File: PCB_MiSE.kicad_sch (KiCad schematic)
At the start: 40 parts, among them IC1 MSP430FR2355TPT, J1 WIFI, J10 Conn_01x01, J11 Conn_01x01, J2 Conn_01x03, J3 Conn_01x01, J4 Clk read conn, J5 Conn_01x01, J6 Display, J7 Conn_01x01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

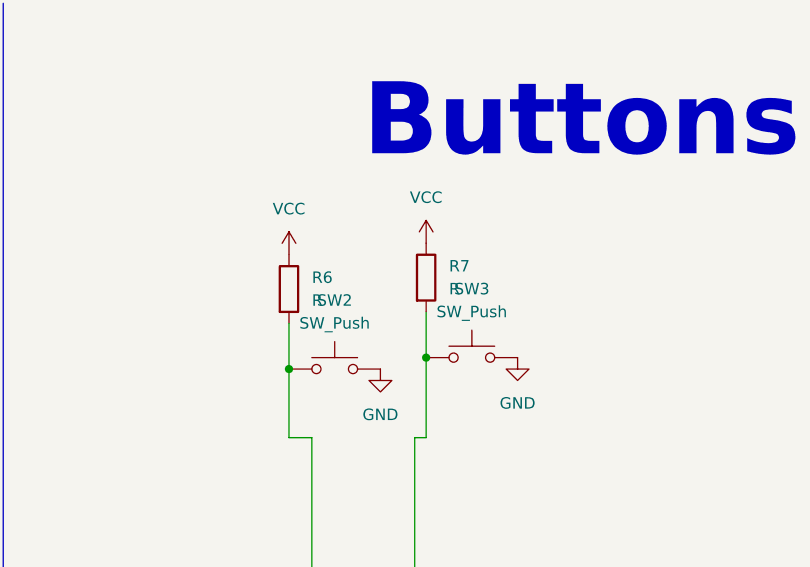
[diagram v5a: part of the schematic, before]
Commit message: falta cambiar pulsadores
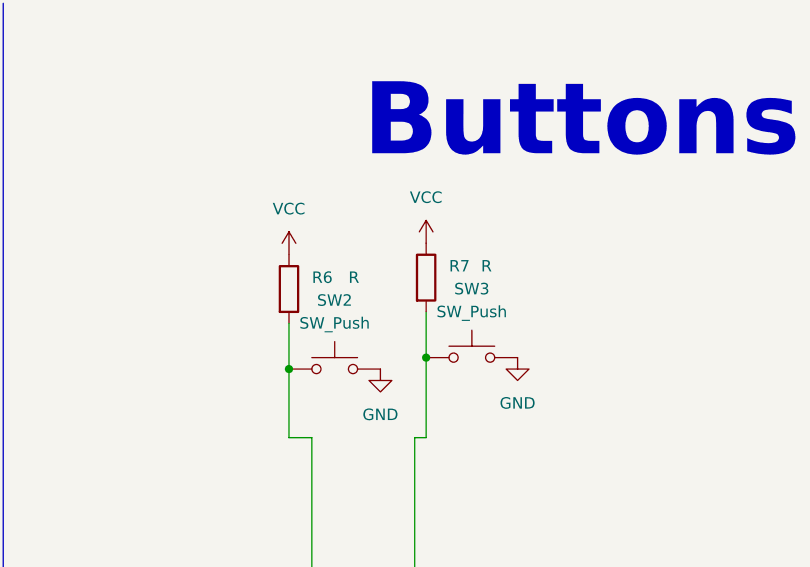
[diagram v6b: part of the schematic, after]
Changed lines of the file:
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@@
 		)
 		(instances
-			(project ""
+			(project "PCB_MiSE"
 				(path "/d767662d-a2fb-4431-89c7-c67b7c23601b"
 					(reference "SW1")
@@
 		(on_board yes)
 		(dnp no)
-		(fields_autoplaced yes)
 		(property "Reference" "R6"
 			(at 323.85 43.1799 0)
@@
 		)
 		(property "Value" "R"
-			(at 323.85 45.7199 0)
+			(at 327.914 43.18 0)
 			(effects
 				(font
@@
 		(on_board yes)
 		(dnp no)
-		(fields_autoplaced yes)
 		(property "Reference" "R7"
 			(at 339.09 41.9099 0)
@@
 		)
 		(property "Value" "R"
-			(at 339.09 44.4499 0)
-			(effects
-				(font
+			(at 342.646 41.91 0)
+			(effects
+				(font

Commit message: MiSE 13/3
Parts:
- R1, R10, R5, R9: value R -> 10k
- R12, R13: value R -> 2k2
- R14, R6, R7: value R -> 1k
- R2: value R -> 31k
- R3: value R -> 20k
- R4: value R -> 47k
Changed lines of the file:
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@@
 			(width 0)
 			(type default)
+			(color 255 0 0 1)
 		)
 	)
@@
 			(width 0)
 			(type default)
+			(color 255 0 0 1)
 		)
 	)
@@
 			(width 0)
 			(type default)
+			(color 255 0 0 1)
 		)
 	)
@@
 			(width 0)
 			(type default)
+			(color 255 0 0 1)
 		)
 	)
@@
 			(width 0)
 			(type default)
+			(color 255 0 0 1)
 		)
 	)
@@
 			(width 0)
 			(type default)
+			(color 255 0 0 1)
 		)
 	)
@@
 			(width 0)
 			(type default)
+			(color 255 0 0 1)
 		)
 	)
@@
 			(width 0)
 			(type default)
+			(color 255 0 0 1)
 		)
 	)
@@
 			(width 0)
 			(type default)
+			(color 255 0 0 1)
 		)
 	)
@@
 			(width 0)
 			(type default)
+			(color 255 0 0 1)
 		)
 	)
@@
 			(width 0)
 			(type default)
+			(color 255 0 0 1)
 		)
 	)
@@
 			(width 0)
 			(type default)
+			(color 255 0 0 1)
 		)
 	)
@@
 			(width 0)
 			(type default)
+			(color 255 0 0 1)
 		)
 	)
@@
 			(width 0)
 			(type default)
+			(color 255 0 0 1)
 		)
 	)
@@
 			(width 0)
 			(type default)
+			(color 255 0 0 1)
 		)
 	)
@@
 			(width 0)
 			(type default)
+			(color 255 0 0 1)
 		)
 	)
@@
 			(width 0)
 			(type default)
+			(color 255 0 0 1)
 		)
 	)
@@
 			(width 0)
 			(type default)
+			(color 255 0 0 1)
 		)
 	)
@@
 			(width 0)
 			(type default)
+			(color 255 0 0 1)
 		)
 	)
@@
 			(width 0)
 			(type default)
+			(color 255 0 0 1)
 		)
 	)
@@
 			(width 0)
 			(type default)
+			(color 255 0 0 1)
 		)
 	)
@@
 			)
 		)
-		(property "Value" "R"
+		(property "Value" "2k2"
 			(at 241.3 186.6899 0)
 			(effects
@@
 			)
 		)
-		(property "Value" "R"
+		(property "Value" "1k"
 			(at 327.914 43.18 0)
 			(effects
@@
 			)
 		)
-		(property "Value" "R"
+		(property "Value" "10k"
 			(at 214.63 87.6299 0)
 			(effects
@@
 		(lib_id "Device:R")
 		(at 29.21 344.17 0)
+		(mirror y)
 		(unit 1)
 		(exclude_from_sim no)
@@
 		(on_board yes)
 		(dnp no)
-		(fields_autoplaced yes)
 		(property "Reference" "R3"
-			(at 31.75 342.8999 0)
+			(at 26.67 342.8999 0)
 			(effects
 				(font
@@
 			)
 		)
-		(property "Value" "R"
-			(at 31.75 345.4399 0)
+		(property "Value" "20k"
+			(at 26.67 345.4399 0)
 			(effects
 				(font
@@
 		)
 		(property "Footprint" "Resistor_SMD:R_0805_2012Metric_Pad1.20x1.40mm_HandSolder"
-			(at 27.432 344.17 90)
+			(at 30.988 344.17 90)
 			(effects
 				(font
@@
 			)
 		)
-		(property "Value" "R"
+		(property "Value" "31k"
 			(at 31.75 309.8799 0)
 			(effects
@@
 			)
 		)
-		(property "Value" "R"
+		(property "Value" "10k"
 			(at 567.69 220.9799 0)
 			(effects
@@
 			)
 		)
-		(property "Value" "R"
+		(property "Value" "1k"
 			(at 342.646 41.91 0)
 			(effects
@@
 			)
 		)
-		(property "Value" "R"
+		(property "Value" "1k"
 			(at 408.94 380.9999 0)
 			(effects
@@
 			)
 		)
-		(property "Value" "R"
+		(property "Value" "47k"
 			(at 213.36 264.1599 0)
 			(effects
@@
 			)
 		)
-		(property "Value" "R"
+		(property "Value" "10k"
 			(at 87.63 205.7399 0)
 			(effects
@@
 			)
 		)
-		(property "Value" "R"
+		(property "Value" "10k"
 			(at 31.75 279.3999 0)
 			(effects
@@
 			)
 		)
-		(property "Value" "R"
+		(property "Value" "2k2"
 			(at 271.78 133.3499 0)
 			(effects

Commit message: Cambios de errores opamp
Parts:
- C3, C4: value 100n -> 12p
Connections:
- net VCC: now also U1.3 (+)
- net at S1.2, U1.2 (-), U1.5 (+): no longer U1.3 (+)
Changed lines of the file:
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@@
 	)
 	(junction
+		(at 29.21 273.05)
+		(diameter 0)
+		(color 0 0 0 0)
+	)
+	(junction
 		(at 278.13 386.08)
 		(diameter 0)
@@
 	)
 	(junction
-		(at 72.39 283.21)
-		(diameter 0)
-		(color 0 0 0 0)
-	)
-	(junction
-		(at 38.1 214.63)
-		(diameter 0)
-		(color 0 0 0 0)
-	)
-	(junction
 		(at 50.8 125.73)
 		(diameter 0)
@@
 	)
 	(junction
+		(at 72.39 278.13)
+		(diameter 0)
+		(color 0 0 0 0)
+	)
+	(junction
 		(at 29.21 337.82)
 		(diameter 0)
@@
 	(wire
 		(pts
-			(xy 72.39 278.13) (xy 72.39 283.21)
-		)
-		(stroke
-			(width 0)
-			(type default)
-		)
-	)
-	(wire
-		(pts
 			(xy 299.72 325.12) (xy 299.72 269.24)
 		)
@@
 	(wire
 		(pts
-			(xy 62.23 254) (xy 63.5 252.73)
+			(xy 293.37 379.73) (xy 299.72 379.73)
 		)
 		(stroke
@@
 	(wire
 		(pts
-			(xy 293.37 379.73) (xy 299.72 379.73)
+			(xy 302.26 137.16) (xy 302.26 144.78)
 		)
 		(stroke
@@
 	(wire
 		(pts
-			(xy 302.26 137.16) (xy 302.26 144.78)
+			(xy 532.13 215.9) (xy 532.13 219.71)
 		)
 		(stroke
@@
 	(wire
 		(pts
-			(xy 532.13 215.9) (xy 532.13 219.71)
+			(xy 29.21 337.82) (xy 74.93 337.82)
 		)
 		(stroke
 			(width 0)
 			(type default)
+			(color 255 0 0 1)
 		)
 	)
 	(wire
 		(pts
-			(xy 29.21 337.82) (xy 74.93 337.82)
+			(xy 29.21 273.05) (xy 29.21 274.32)
 		)
 		(stroke
@@
 	(wire
 		(pts
+			(xy 29.21 266.7) (xy 29.21 273.05)
+		)
+		(stroke
+			(width 0)
+			(type default)
+			(color 255 0 0 1)
+		)
+	)
+	(wire
+		(pts
 			(xy 205.74 256.54) (xy 205.74 266.7)
 		)
@@
 	(wire
 		(pts
-			(xy 33.02 214.63) (xy 33.02 254)
-		)
-		(stroke
-			(width 0)
-			(type default)
-		)
-	)
-	(wire
-		(pts
 			(xy 233.68 167.64) (xy 233.68 193.04)
 		)
@@
 	(wire
 		(pts
-			(xy 210.82 231.14) (xy 213.36 231.14)
+			(xy 38.1 214.63) (xy 38.1 278.13)
 		)
 		(stroke
@@
 	(wire
 		(pts
-			(xy 29.21 266.7) (xy 29.21 274.32)
+			(xy 210.82 231.14) (xy 213.36 231.14)
 		)
 		(stroke
 			(width 0)
 			(type default)
-			(color 255 0 0 1)
 		)
 	)
@@
 	(wire
 		(pts
-			(xy 38.1 273.05) (xy 74.93 273.05)
-		)
-		(stroke
-			(width 0)
-			(type default)
-		)
-	)
-	(wire
-		(pts
 			(xy 322.58 378.46) (xy 341.63 378.46)
 		)
@@
 	(wire
 		(pts
-			(xy 38.1 214.63) (xy 38.1 273.05)
-		)
-		(stroke
-			(width 0)
-			(type default)
-		)
-	)
-	(wire
-		(pts
 			(xy 403.86 119.38) (xy 403.86 198.12)
 		)
@@
 	(wire
 		(pts
-			(xy 72.39 283.21) (xy 72.39 332.74)
+			(xy 72.39 278.13) (xy 72.39 332.74)
 		)
 		(stroke
@@
 	(wire
 		(pts
-			(xy 63.5 252.73) (xy 63.5 283.21)
-		)
-		(stroke
-			(width 0)
-			(type default)
-		)
-	)
-	(wire
-		(pts
 			(xy 185.42 256.54) (xy 205.74 256.54)
 		)
@@
 	(wire
 		(pts
-			(xy 33.02 214.63) (xy 38.1 214.63)
-		)
-		(stroke
-			(width 0)
-			(type default)
-		)
-	)
-	(wire
-		(pts
 			(xy 72.39 332.74) (xy 74.93 332.74)
 		)
@@
 	(wire
 		(pts
-			(xy 63.5 283.21) (xy 72.39 283.21)
+			(xy 38.1 278.13) (xy 72.39 278.13)
 		)
 		(stroke
@@
 	(wire
 		(pts
-			(xy 33.02 254) (xy 62.23 254)
-		)
-		(stroke
-			(width 0)
-			(type default)
-		)
-	)
-	(wire
-		(pts
 			(xy 186.69 273.05) (xy 186.69 270.51)
 		)
@@
 	(wire
 		(pts
+			(xy 29.21 273.05) (xy 74.93 273.05)
+		)
+		(stroke
+			(width 0)
+			(type default)
+		)
+	)
+	(wire
+		(pts
 			(xy 269.24 123.19) (xy 269.24 128.27)
 		)
@@
 			)
 		)
-		(property "Value" "100n"
+		(property "Value" "12p"
 			(at 216.408 237.744 0)
 			(effects
@@
 		)
 		(property "Value" "LMV324"
-			(at 64.262 304.8 0)
+			(at 62.23 307.848 0)
 			(effects
 				(font
@@
 			)
 		)
-		(property "Value" "100n"
+		(property "Value" "12p"
 			(at 191.77 237.744 0)
 			(effects
@@
 		(on_board yes)
 		(dnp no)
-		(fields_autoplaced yes)
 		(property "Reference" "U1"
 			(at 82.55 265.43 0)
